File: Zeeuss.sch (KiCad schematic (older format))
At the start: 30 parts, among them J2 Conn_01x05_Male, SW1 SW_SPST, U1 MP20045, U2 IP5306

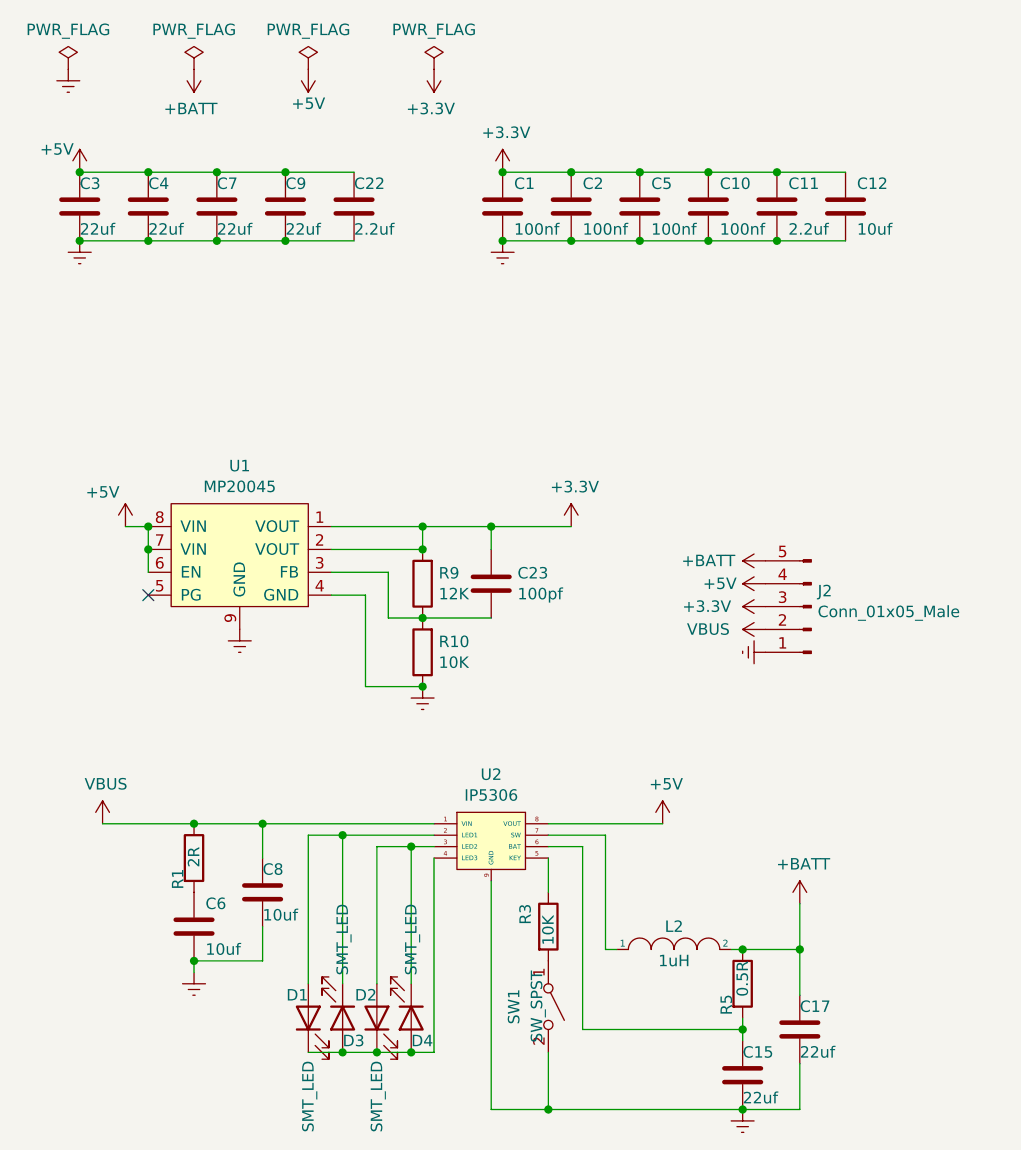
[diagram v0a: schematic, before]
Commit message: 2.0版本，删掉一些滤波电容，引出充电led引脚，取消自带led，引出开关，利用单片机控制开关，PCB重新布局
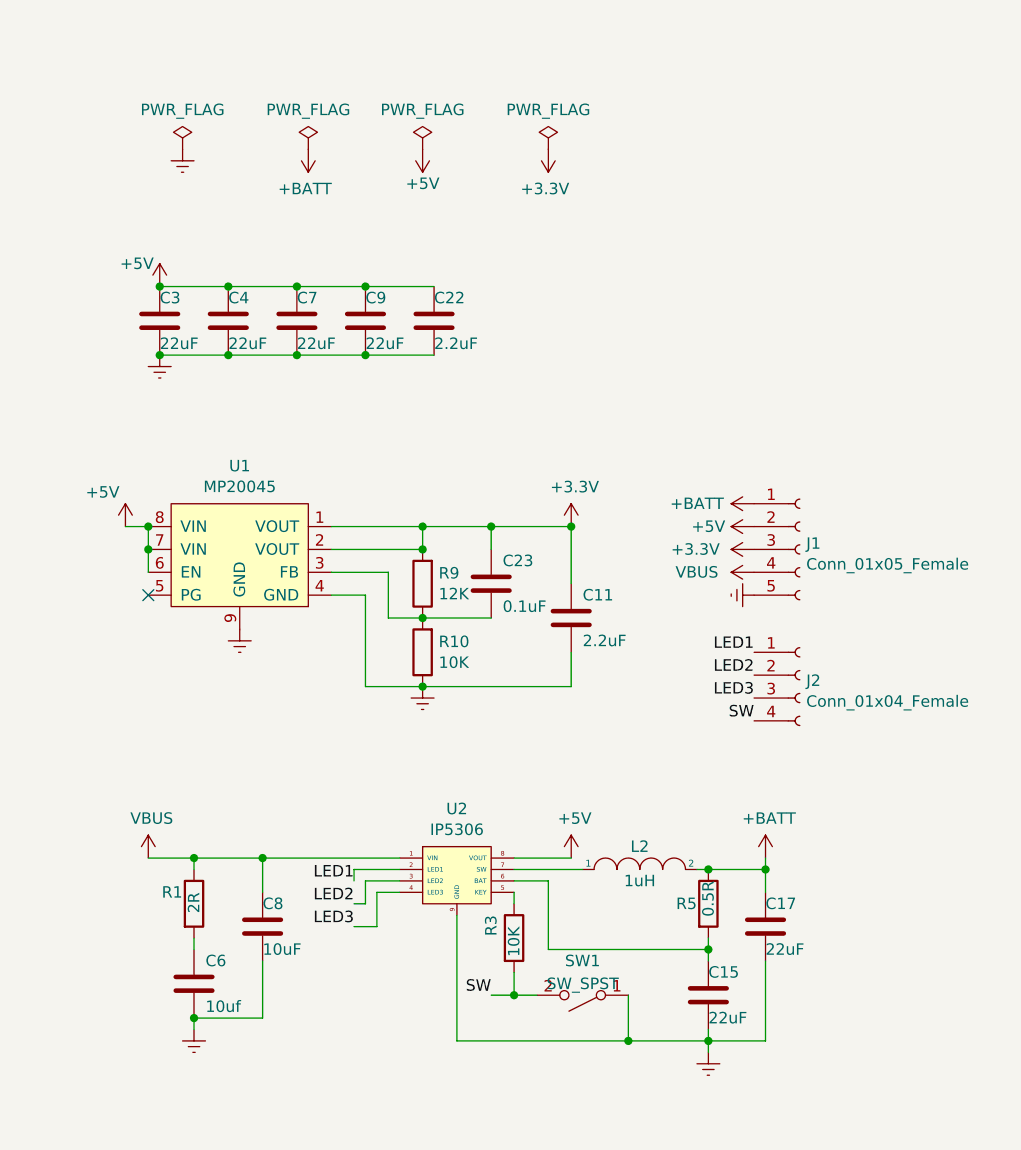
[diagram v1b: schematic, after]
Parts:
- removed C1, C10, C2, C5: 100nf, Capacitor_SMD:C_0603_1608Metric_Pad1.05x0.95mm_HandSolder, symbol Device:C
- removed C12: 10uf, Capacitor_SMD:C_0603_1608Metric_Pad1.05x0.95mm_HandSolder, symbol Device:C
- removed D1, D2, D3, D4: SMT_LED, LED_SMD:LED_0603_1608Metric, symbol Device:LED
- removed J2: Conn_01x05_Male, Connector_PinHeader_2.00mm:PinHeader_1x05_P2.00mm_Vertical_SMD_Pin1Right, symbol Connector:Conn_01x05_Male
- added J1: Conn_01x05_Female, Connector_PinHeader_2.00mm:PinHeader_1x05_P2.00mm_Vertical, symbol Connector:Conn_01x05_Female
- added J2: Conn_01x04_Female, Connector_PinHeader_2.00mm:PinHeader_1x04_P2.00mm_Vertical, symbol Connector:Conn_01x04_Female
- C11, C22: value 2.2uf -> 2.2uF
- C15, C17, C3, C4, C7, C9: value 22uf -> 22uF
- C23: value 100pf -> 0.1uF
- C8: value 10uf -> 10uF
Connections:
- net +3V3: now also J1.3 (Pin_3)
- net +5V: now also J1.2 (Pin_2)
- net +BATT: now also J1.1 (Pin_1)
- net Earth: now also SW1.1 (A), J1.5 (Pin_5); no longer SW1.2 (B)
- net VBUS: now also J1.4 (Pin_4)
- net SW: now reaches R3.2
- net SW: now also SW1.2 (B), J2.4 (Pin_4); no longer SW1.1 (A)
- net LED3: now reaches U2.4 (LED3)
- net LED3: now also J2.3 (Pin_3)
- net LED1: now reaches U2.2 (LED1)
- net LED1: now also J2.1 (Pin_1)
- net LED2: now reaches U2.3 (LED2)
- net LED2: now also J2.2 (Pin_2)
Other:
- moved on the sheet: C11, C15, C17, C22, C3, C4, C6, C7, C8, C9, L2, R1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

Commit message: 更新文档，gerber
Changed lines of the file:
@@
 Comment4 ""
 $EndDescr
-$Comp
-L power:PWR_FLAG #FLG01
-U 1 1 5F0122A3
-P 1200 1100
-F 0 "#FLG01" H 1200 1175 50  0001 C CNN
-F 1 "PWR_FLAG" H 1200 1273 50  0000 C CNN
-F 2 "" H 1200 1100 50  0001 C CNN
-F 3 "~" H 1200 1100 50  0001 C CNN
-	1    1200 1100
-	1    0    0    -1
-$EndComp
-$Comp
-L power:PWR_FLAG #FLG02
-U 1 1 5F6633B1
-P 1750 1100
-F 0 "#FLG02" H 1750 1175 50  0001 C CNN
-F 1 "PWR_FLAG" H 1750 1273 50  0000 C CNN
-F 2 "" H 1750 1100 50  0001 C CNN
-F 3 "~" H 1750 1100 50  0001 C CNN
-	1    1750 1100
-	1    0    0    -1
-$EndComp
-$Comp
-L power:+BATT #PWR03
-U 1 1 5F664054
-P 1750 1100
-F 0 "#PWR03" H 1750 950 50  0001 C CNN
-F 1 "+BATT" H 1765 1273 50  0000 C CNN
-F 2 "" H 1750 1100 50  0001 C CNN
-F 3 "" H 1750 1100 50  0001 C CNN
-	1    1750 1100
-	-1   0    0    1
-$EndComp
 Wire Wire Line
 	2650 4300 2800 4300
@@
 	3750 4200 3750 4250
 Connection ~ 3750 4250
-$Comp
-L power:+5V #PWR0111
-U 1 1 5FA025DD
-P 2250 1100
-F 0 "#PWR0111" H 2250 950 50  0001 C CNN
-F 1 "+5V" H 2250 1250 50  0000 C CNN
-F 2 "" H 2250 1100 50  0001 C CNN
-F 3 "" H 2250 1100 50  0001 C CNN
-	1    2250 1100
-	-1   0    0    1
-$EndComp
-$Comp
-L power:PWR_FLAG #FLG0101
-U 1 1 5FA03890
-P 2250 1100
-F 0 "#FLG0101" H 2250 1175 50  0001 C CNN
-F 1 "PWR_FLAG" H 2250 1273 50  0000 C CNN
-F 2 "" H 2250 1100 50  0001 C CNN
-F 3 "~" H 2250 1100 50  0001 C CNN
-	1    2250 1100
-	1    0    0    -1
-$EndComp
-$Comp
-L power:Earth #PWR0112
-U 1 1 5FA05B43
-P 1200 1100
-F 0 "#PWR0112" H 1200 850 50  0001 C CNN
-F 1 "Earth" H 1200 950 50  0001 C CNN
-F 2 "" H 1200 1100 50  0001 C CNN
-F 3 "~" H 1200 1100 50  0001 C CNN
-	1    1200 1100
-	1    0    0    -1
-$EndComp
 Wire Wire Line
 	1050 2850 1050 2950
 Connection ~ 1050 2850
-$Comp
-L power:PWR_FLAG #FLG0102
-U 1 1 5FA08AED
-P 2800 1100
-F 0 "#FLG0102" H 2800 1175 50  0001 C CNN
-F 1 "PWR_FLAG" H 2800 1273 50  0000 C CNN
-F 2 "" H 2800 1100 50  0001 C CNN
-F 3 "~" H 2800 1100 50  0001 C CNN
-	1    2800 1100
-	1    0    0    -1
-$EndComp
-$Comp
-L power:+3.3V #PWR0113
-U 1 1 5FA09A07
-P 2800 1100
-F 0 "#PWR0113" H 2800 950 50  0001 C CNN
-F 1 "+3.3V" H 2815 1273 50  0000 C CNN
-F 2 "" H 2800 1100 50  0001 C CNN
-F 3 "" H 2800 1100 50  0001 C CNN
-	1    2800 1100
-	-1   0    0    1
-$EndComp
 Connection ~ 1100 2000
 Connection ~ 1100 1700
